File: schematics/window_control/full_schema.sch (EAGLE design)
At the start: 75 parts, among them J1 MTR-SERVO-FS5103B, J10 USBASP_PIN, J2 J2, J3 J2, J4 J2, J5 J2, J6 J2, J7 J2, J8 J2, J9 J2, Q1 2N3904, Q2 2N3904, Q3 2N3906BU, Q4 2N3904, Q5 STP14NM50N, SW1 SWITCH, U1 ESP32, U2 LM311P, U3 NE555P, U4 SN74LS32N, U5 BMP280 / 5V, U6 ATMEGA328P, U7 LM317L, U8 GY-SGP30, U9 LM358, X1 HC-49S (16MHZ)

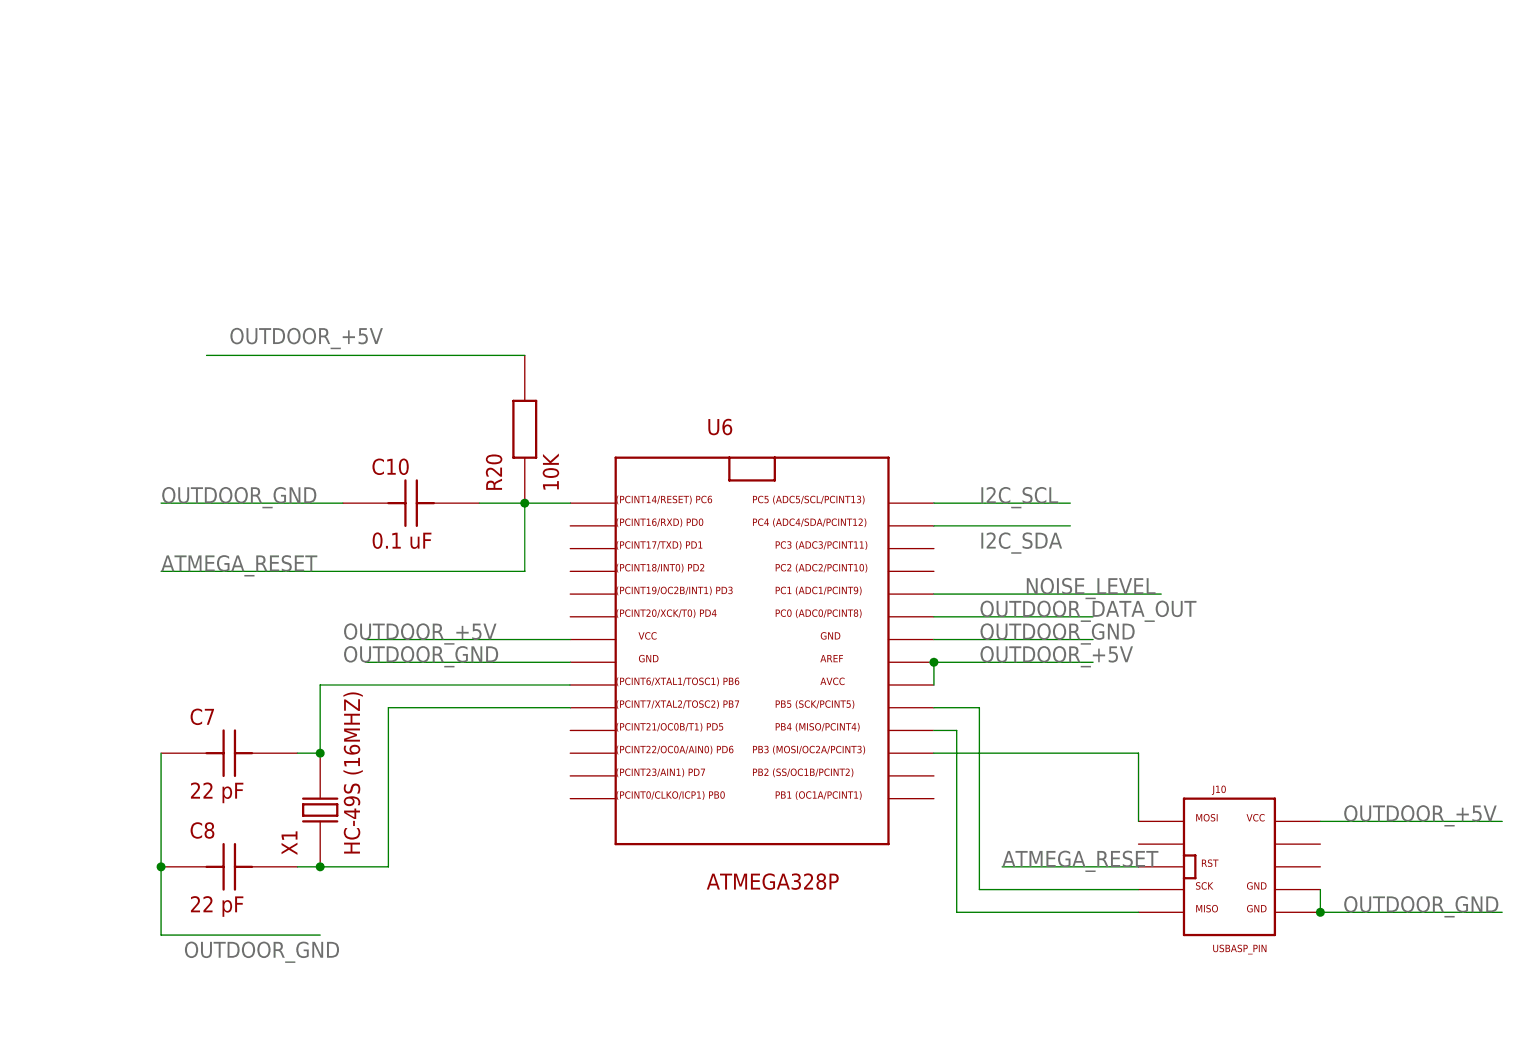
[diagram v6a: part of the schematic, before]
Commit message: Added TX and RX links from USBASP to ATMEGA
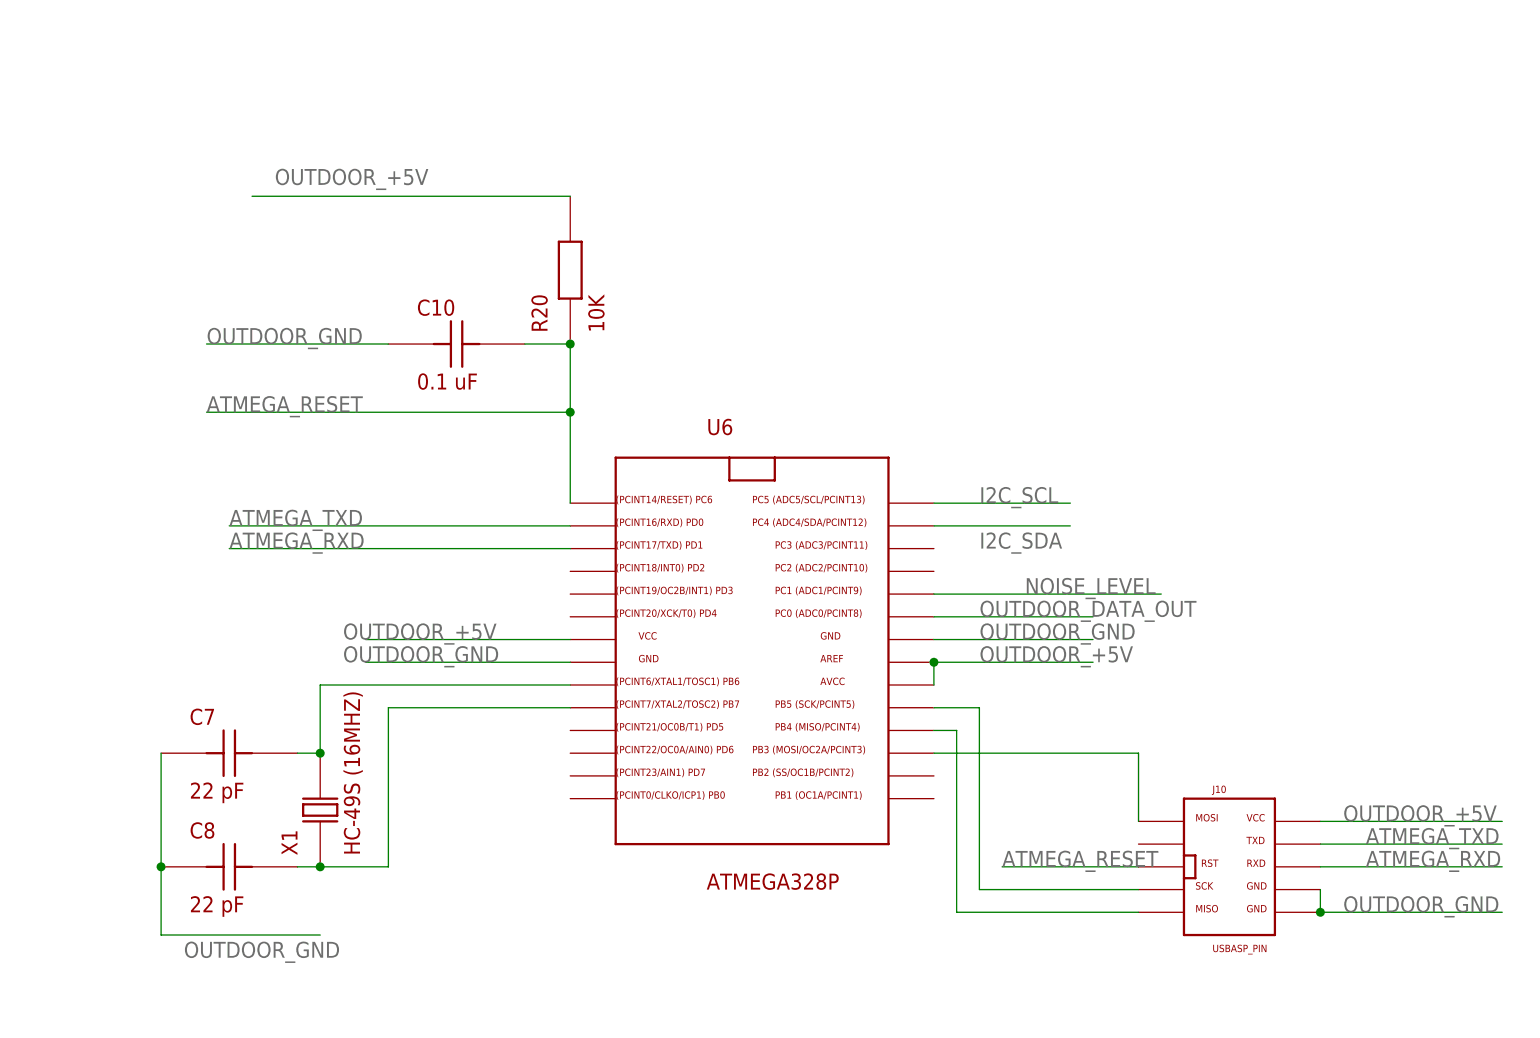
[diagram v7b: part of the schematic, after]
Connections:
- new net ATMEGA_RXD: J10.RXD, U6.PD1
- new net ATMEGA_TXD: J10.TXD, U6.PD0
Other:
- moved on the sheet: C10, R20
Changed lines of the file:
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@@
 <attribute name="NAME" x="-33.02" y="-10.16" size="1.778" layer="94"/>
 </instance>
-<instance part="R20" gate="G$1" x="254" y="152.4" smashed="yes" rot="R90" grouprefs="ATMEGA32">
-<attribute name="NAME" x="251.46" y="146.05" size="1.778" layer="94" rot="R90"/>
-<attribute name="VALUE" x="257.81" y="146.05" size="1.778" layer="94" rot="R90"/>
+<instance part="R20" gate="G$1" x="259.08" y="170.18" smashed="yes" rot="R90" grouprefs="ATMEGA32">
+<attribute name="NAME" x="256.54" y="163.83" size="1.778" layer="94" rot="R90"/>
+<attribute name="VALUE" x="262.89" y="163.83" size="1.778" layer="94" rot="R90"/>
 </instance>
 <instance part="U5" gate="G$1" x="190.5" y="228.6" smashed="yes" grouprefs="BME_280_TEMP_HUM1">
@@
 <attribute name="VALUE" x="274.32" y="101.6" size="1.778" layer="94"/>
 </instance>
-<instance part="C10" gate="G$1" x="241.3" y="144.78" smashed="yes" grouprefs="ATMEGA32">
-<attribute name="NAME" x="236.855" y="147.955" size="1.778" layer="94"/>
-<attribute name="VALUE" x="236.855" y="139.7" size="1.778" layer="94"/>
+<instance part="C10" gate="G$1" x="246.38" y="162.56" smashed="yes" grouprefs="ATMEGA32">
+<attribute name="NAME" x="241.935" y="165.735" size="1.778" layer="94"/>
+<attribute name="VALUE" x="241.935" y="157.48" size="1.778" layer="94"/>
 </instance>
 <instance part="J10" gate="G$1" x="332.74" y="104.14" smashed="yes" grouprefs="ATMEGA32">
@@
 <segment>
 <pinref part="R20" gate="G$1" pin="P$2"/>
-<wire x1="254" y1="161.29" x2="218.44" y2="161.29" width="0.1524" layer="91" grouprefs="ATMEGA32"/>
-<label x="220.98" y="162.56" size="1.778" layer="95" grouprefs="ATMEGA32"/>
+<wire x1="259.08" y1="179.07" x2="223.52" y2="179.07" width="0.1524" layer="91" grouprefs="ATMEGA32"/>
+<label x="226.06" y="180.34" size="1.778" layer="95" grouprefs="ATMEGA32"/>
 </segment>
 <segment>
@@
 </segment>
 <segment>
-<wire x1="233.68" y1="144.78" x2="213.36" y2="144.78" width="0.1524" layer="91" grouprefs="ATMEGA32"/>
-<label x="213.36" y="144.78" size="1.778" layer="95" grouprefs="ATMEGA32"/>
+<wire x1="238.76" y1="162.56" x2="218.44" y2="162.56" width="0.1524" layer="91" grouprefs="ATMEGA32"/>
+<label x="218.44" y="162.56" size="1.778" layer="95" grouprefs="ATMEGA32"/>
 <pinref part="C10" gate="G$1" pin="P$1"/>
 </segment>
@@
 </segment>
 <segment>
+<wire x1="254" y1="162.56" x2="259.08" y2="162.56" width="0.1524" layer="91" grouprefs="ATMEGA32"/>
+<pinref part="R20" gate="G$1" pin="P$1"/>
+<junction x="259.08" y="162.56" grouprefs="ATMEGA32"/>
+<pinref part="C10" gate="G$1" pin="P$2"/>
+<wire x1="218.44" y1="154.94" x2="259.08" y2="154.94" width="0.1524" layer="91" grouprefs="ATMEGA32"/>
+<wire x1="259.08" y1="154.94" x2="259.08" y2="162.56" width="0.1524" layer="91" grouprefs="ATMEGA32"/>
+<label x="218.44" y="154.94" size="1.778" layer="95" grouprefs="ATMEGA32"/>
 <pinref part="U6" gate="G$1" pin="PC6"/>
-<wire x1="248.92" y1="144.78" x2="254" y2="144.78" width="0.1524" layer="91" grouprefs="ATMEGA32"/>
-<pinref part="R20" gate="G$1" pin="P$1"/>
-<wire x1="254" y1="144.78" x2="259.08" y2="144.78" width="0.1524" layer="91" grouprefs="ATMEGA32"/>
-<junction x="254" y="144.78" grouprefs="ATMEGA32"/>
-<pinref part="C10" gate="G$1" pin="P$2"/>
-<wire x1="213.36" y1="137.16" x2="254" y2="137.16" width="0.1524" layer="91" grouprefs="ATMEGA32"/>
-<wire x1="254" y1="137.16" x2="254" y2="144.78" width="0.1524" layer="91" grouprefs="ATMEGA32"/>
-<label x="213.36" y="137.16" size="1.778" layer="95" grouprefs="ATMEGA32"/>
-</segment>
-</net>
+<wire x1="259.08" y1="144.78" x2="259.08" y2="154.94" width="0.1524" layer="91" grouprefs="ATMEGA32"/>
+<junction x="259.08" y="154.94" grouprefs="ATMEGA32"/>
+</segment>
+</net>
+<net name="ATMEGA_TXD" class="0">
+<segment>
+<pinref part="J10" gate="G$1" pin="TXD"/>
+<wire x1="342.9" y1="106.68" x2="363.22" y2="106.68" width="0.1524" layer="91" grouprefs="ATMEGA32"/>
+<label x="347.98" y="106.68" size="1.778" layer="95" grouprefs="ATMEGA32"/>
+</segment>
+<segment>
+<pinref part="U6" gate="G$1" pin="PD0"/>
+<wire x1="259.08" y1="142.24" x2="220.98" y2="142.24" width="0.1524" layer="91" grouprefs="ATMEGA32"/>
+<label x="220.98" y="142.24" size="1.778" layer="95" grouprefs="ATMEGA32"/>
+</segment>
+</net>
+<net name="ATMEGA_RXD" class="0">
+<segment>
+<pinref part="J10" gate="G$1" pin="RXD"/>
+<wire x1="342.9" y1="104.14" x2="363.22" y2="104.14" width="0.1524" layer="91" grouprefs="ATMEGA32"/>
+<label x="347.98" y="104.14" size="1.778" layer="95" grouprefs="ATMEGA32"/>
+</segment>
+<segment>
+<pinref part="U6" gate="G$1" pin="PD1"/>
+<wire x1="259.08" y1="139.7" x2="220.98" y2="139.7" width="0.1524" layer="91" grouprefs="ATMEGA32"/>
+<label x="220.98" y="139.7" size="1.778" layer="95" grouprefs="ATMEGA32"/>
+</segment>
+</net>

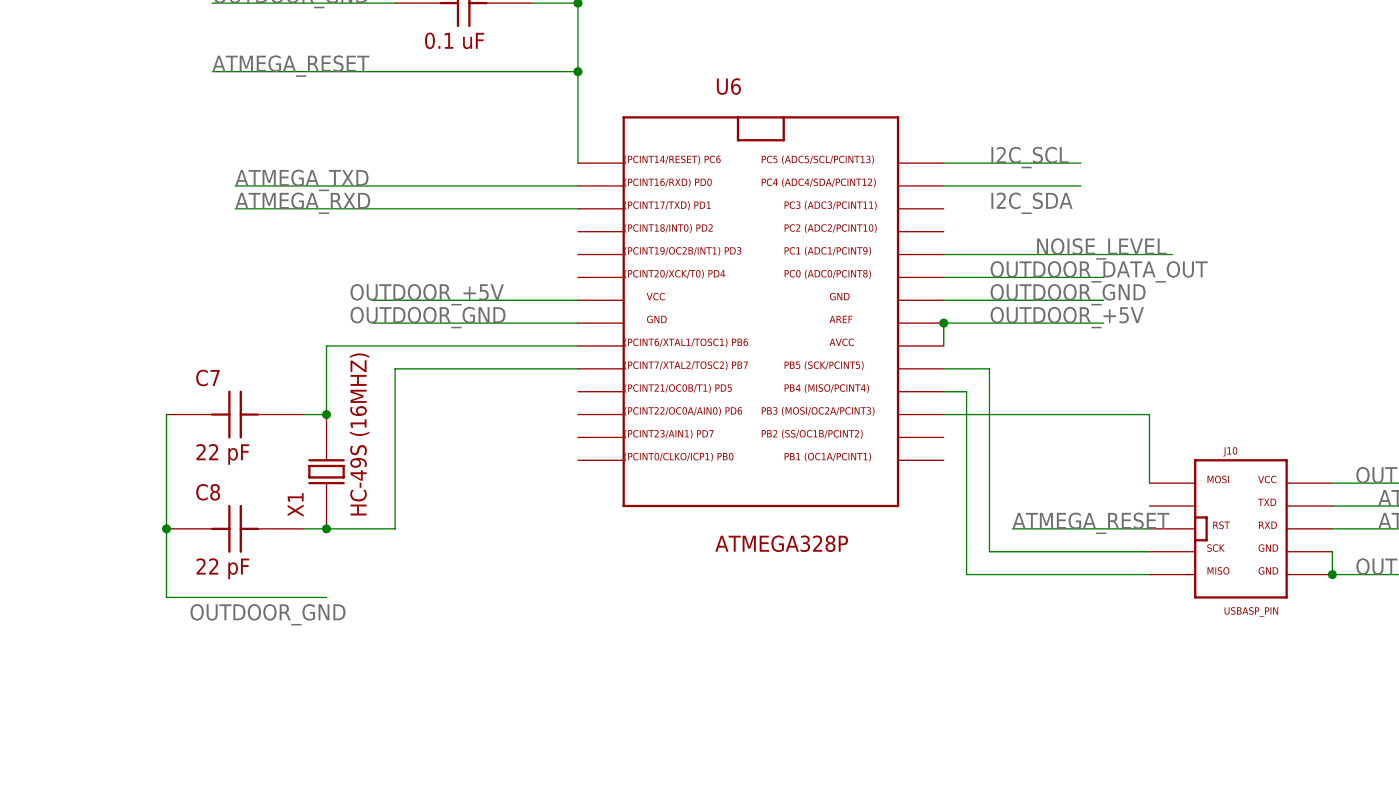
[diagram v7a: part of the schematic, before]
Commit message: Firmware and ATMega connection are synchronized. USBasp works successfully
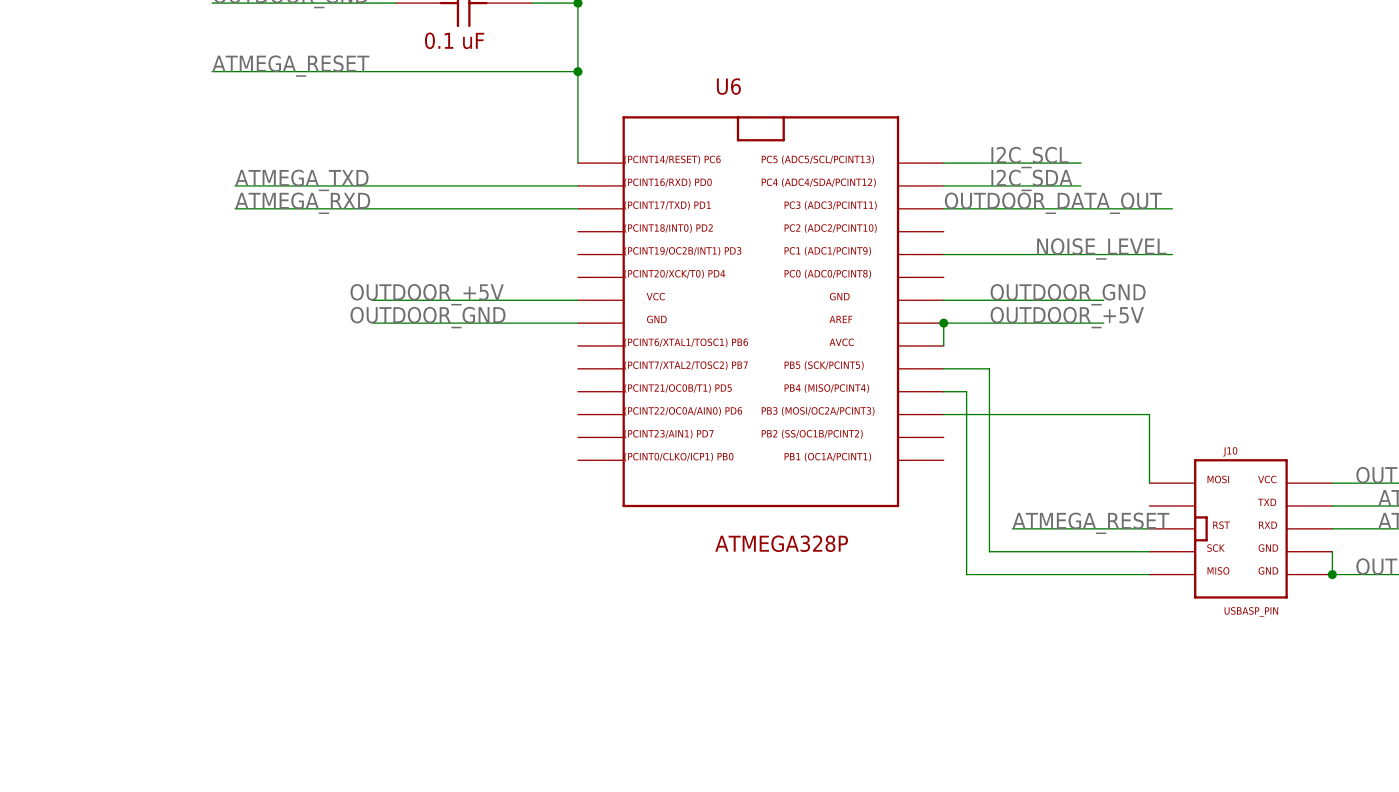
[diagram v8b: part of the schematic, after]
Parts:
- removed C7, C8: 22 pF, my_devices:C-1
- removed X1: HC-49S (16MHZ), my_devices:X
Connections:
- removed net N$22: C7.P$2, U6.PB6, X1.P$2
- removed net N$23: C8.P$2, U6.PB7, X1.P$1
- net OUTDOOR_DATA_OUT: now also U6.PC3; no longer U6.PC0
- net OUTDOOR_GND: no longer C7.P$1, C8.P$1
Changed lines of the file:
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@@
 <part name="U5" library="my_devices" deviceset="BME280" device="" value="BMP280 / 5V"/>
 <part name="U8" library="my_devices" deviceset="GY-SGP30" device=""/>
-<part name="X1" library="my_devices" deviceset="X" device="" value="HC-49S (16MHZ)"/>
-<part name="C7" library="my_devices" deviceset="C-1" device="" value="22 pF"/>
-<part name="C8" library="my_devices" deviceset="C-1" device="" value="22 pF"/>
 <part name="B1" library="my_devices" deviceset="HALL_SENSOR" device="" value="A3144"/>
 <part name="GND10" library="supply1" library_urn="urn:adsk.eagle:library:371" deviceset="GND" device=""/>
@@
 <attribute name="NAME" x="289.56" y="241.3" size="1.778" layer="94"/>
 </instance>
-<instance part="X1" gate="G$1" x="231.14" y="110.49" smashed="yes" rot="R90" grouprefs="ATMEGA32">
-<attribute name="NAME" x="228.6" y="105.41" size="1.778" layer="94" rot="R90"/>
-<attribute name="VALUE" x="235.585" y="105.41" size="1.778" layer="94" rot="R90"/>
-</instance>
-<instance part="C7" gate="G$1" x="220.98" y="116.84" smashed="yes" grouprefs="ATMEGA32">
-<attribute name="NAME" x="216.535" y="120.015" size="1.778" layer="94"/>
-<attribute name="VALUE" x="216.535" y="111.76" size="1.778" layer="94"/>
-</instance>
-<instance part="C8" gate="G$1" x="220.98" y="104.14" smashed="yes" grouprefs="ATMEGA32">
-<attribute name="NAME" x="216.535" y="107.315" size="1.778" layer="94"/>
-<attribute name="VALUE" x="216.535" y="99.06" size="1.778" layer="94"/>
-</instance>
 <instance part="B1" gate="G$1" x="-53.34" y="66.04" smashed="yes" grouprefs="HALL_SENSOR">
 <attribute name="NAME" x="-45.72" y="66.04" size="1.778" layer="94"/>
@@
 </segment>
 <segment>
-<pinref part="C7" gate="G$1" pin="P$1"/>
-<pinref part="C8" gate="G$1" pin="P$1"/>
-<wire x1="213.36" y1="116.84" x2="213.36" y2="104.14" width="0.1524" layer="91" grouprefs="ATMEGA32"/>
-<wire x1="213.36" y1="96.52" x2="231.14" y2="96.52" width="0.1524" layer="91" grouprefs="ATMEGA32"/>
-<wire x1="213.36" y1="104.14" x2="213.36" y2="96.52" width="0.1524" layer="91" grouprefs="ATMEGA32"/>
-<junction x="213.36" y="104.14" grouprefs="ATMEGA32"/>
-<label x="215.9" y="93.98" size="1.778" layer="95" grouprefs="ATMEGA32"/>
-</segment>
-<segment>
 <pinref part="J10" gate="G$1" pin="GND"/>
 <pinref part="J10" gate="G$1" pin="GND1"/>
@@
 <segment>
 <wire x1="299.72" y1="142.24" x2="314.96" y2="142.24" width="0.1524" layer="91" grouprefs="ATMEGA32"/>
-<label x="304.8" y="139.7" size="1.778" layer="95" grouprefs="ATMEGA32"/>
+<label x="304.8" y="142.24" size="1.778" layer="95" grouprefs="ATMEGA32"/>
 <pinref part="U6" gate="G$1" pin="PC4"/>
 </segment>
@@
 <net name="OUTDOOR_DATA_OUT" class="0">
 <segment>
-<wire x1="299.72" y1="132.08" x2="317.5" y2="132.08" width="0.1524" layer="91" grouprefs="ATMEGA32"/>
-<label x="304.8" y="132.08" size="1.778" layer="95" grouprefs="ATMEGA32"/>
-<pinref part="U6" gate="G$1" pin="PC0"/>
-</segment>
-<segment>
 <pinref part="J6" gate="G$1" pin="PIN_1"/>
 <wire x1="144.78" y1="116.84" x2="172.72" y2="116.84" width="0.1524" layer="91" grouprefs="INDOOR_TO_OUTDOOR_CABEL"/>
 <label x="152.4" y="116.84" size="1.778" layer="95" grouprefs="INDOOR_TO_OUTDOOR_CABEL"/>
+</segment>
+<segment>
+<pinref part="U6" gate="G$1" pin="PC3"/>
+<wire x1="299.72" y1="139.7" x2="325.12" y2="139.7" width="0.1524" layer="91" grouprefs="ATMEGA32"/>
+<label x="299.72" y="139.7" size="1.778" layer="95" grouprefs="ATMEGA32"/>
 </segment>
 </net>
@@
 </segment>
 </net>
-<net name="N$22" class="0">
-<segment>
-<pinref part="C7" gate="G$1" pin="P$2"/>
-<pinref part="X1" gate="G$1" pin="P$2"/>
-<wire x1="228.6" y1="116.84" x2="231.14" y2="116.84" width="0.1524" layer="91" grouprefs="ATMEGA32"/>
-<pinref part="U6" gate="G$1" pin="PB6"/>
-<wire x1="231.14" y1="116.84" x2="231.14" y2="124.46" width="0.1524" layer="91" grouprefs="ATMEGA32"/>
-<wire x1="231.14" y1="124.46" x2="259.08" y2="124.46" width="0.1524" layer="91" grouprefs="ATMEGA32"/>
-<junction x="231.14" y="116.84" grouprefs="ATMEGA32"/>
-</segment>
-</net>
-<net name="N$23" class="0">
-<segment>
-<pinref part="C8" gate="G$1" pin="P$2"/>
-<pinref part="X1" gate="G$1" pin="P$1"/>
-<wire x1="228.6" y1="104.14" x2="231.14" y2="104.14" width="0.1524" layer="91" grouprefs="ATMEGA32"/>
-<wire x1="231.14" y1="104.14" x2="238.76" y2="104.14" width="0.1524" layer="91" grouprefs="ATMEGA32"/>
-<junction x="231.14" y="104.14" grouprefs="ATMEGA32"/>
-<wire x1="238.76" y1="104.14" x2="238.76" y2="121.92" width="0.1524" layer="91" grouprefs="ATMEGA32"/>
-<pinref part="U6" gate="G$1" pin="PB7"/>
-<wire x1="238.76" y1="121.92" x2="259.08" y2="121.92" width="0.1524" layer="91" grouprefs="ATMEGA32"/>
-</segment>
-</net>
